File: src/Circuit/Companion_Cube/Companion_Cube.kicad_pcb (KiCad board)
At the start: 2 copper layers, 43.2 x 43.2 mm, 21 parts, among them CON1 AVR-ISP-6, IC1 ATTINY85-S, P1 LED_4, P2 LED_3, P3 LED_2, P4 LED_1, P5 CONN_1, P6 CONN_1, P7 CONN_1, U1 MINI-B_USB

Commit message: Reorganizing
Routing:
- net GND: track 0.00 -> 2.89 mm
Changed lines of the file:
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@@
   (general
     (links 41)
-    (no_connects 1)
+    (no_connects 0)
     (area 175.609956 109.169999 221.3356 152.450001)
     (thickness 1.6)
     (drawings 12)
-    (tracks 76)
+    (tracks 78)
     (zones 0)
     (modules 21)
@@
     (visible_elements 7FFFFFFF)
     (pcbplotparams
-      (layerselection 3178497)
+      (layerselection 284196865)
       (usegerberextensions true)
       (excludeedgelayer true)
@@
       (plotinvisibletext false)
       (padsonsilk false)
-      (subtractmaskfromsilk false)
+      (subtractmaskfromsilk true)
       (outputformat 1)
       (mirror false)
-      (drillshape 1)
+      (drillshape 0)
       (scaleselection 1)
-      (outputdirectory ""))
+      (outputdirectory S:/Users/TyDesktop/Documents/GitHub/3D-LED-Companion-Cube/src/Circuit/Boards/Main/Gerber/))
   )
   (net 0 "")
@@
   (gr_line (start 206.375 139.065) (end 207.645 139.065) (angle 90) (layer Edge.Cuts) (width 0.1))
   (gr_line (start 191.135 139.065) (end 206.375 139.065) (angle 90) (layer Edge.Cuts) (width 0.1))
+  (segment (start 185.05932 132.4102) (end 185.05932 135.16102) (width 0.55) (layer F.Cu) (net 1))
+  (segment (start 185.05932 135.16102) (end 184.96026 135.26008) (width 0.55) (layer F.Cu) (net 1))
   (segment (start 209.55 130.175) (end 209.55 127) (width 0.254) (layer B.Cu) (net 2))
   (segment (start 198.755 120.65) (end 195.58 120.65) (width 0.254) (layer B.Cu) (net 3))

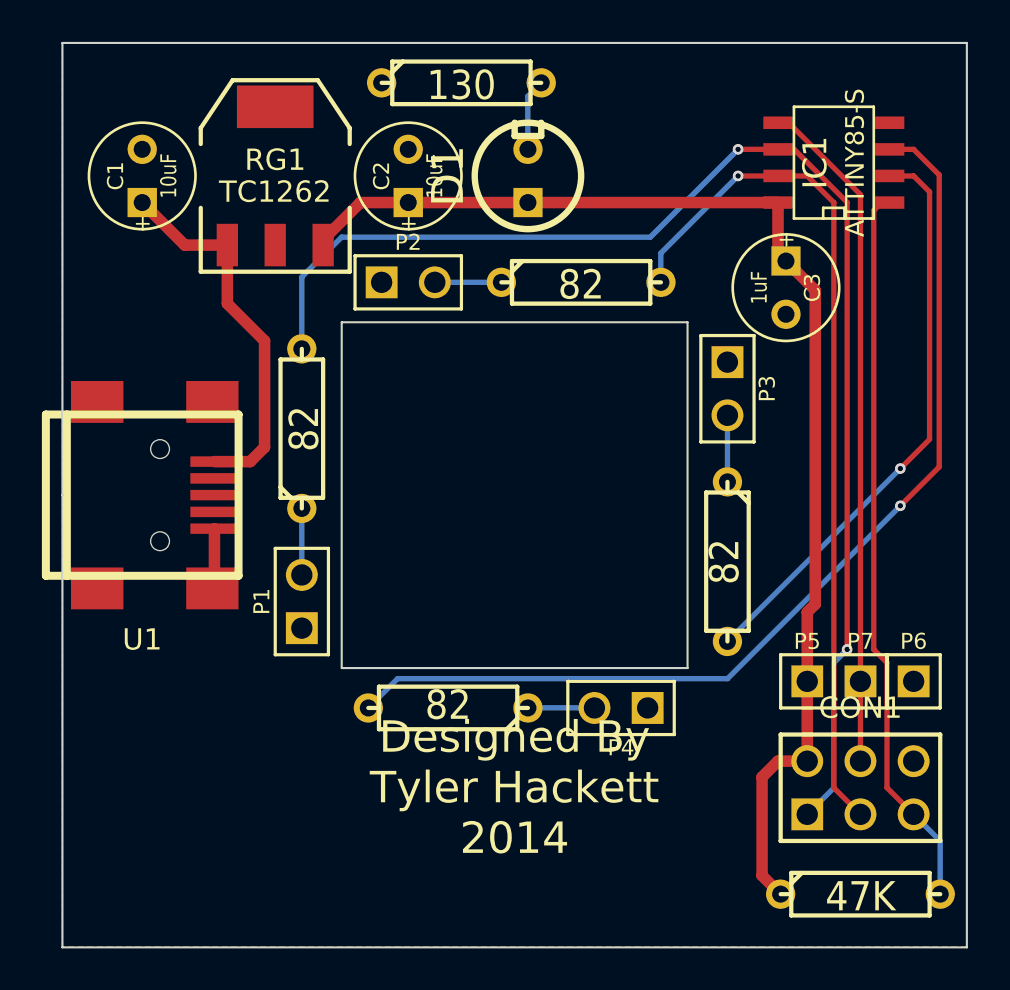
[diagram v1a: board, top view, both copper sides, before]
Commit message: Added attiny85 DIP version
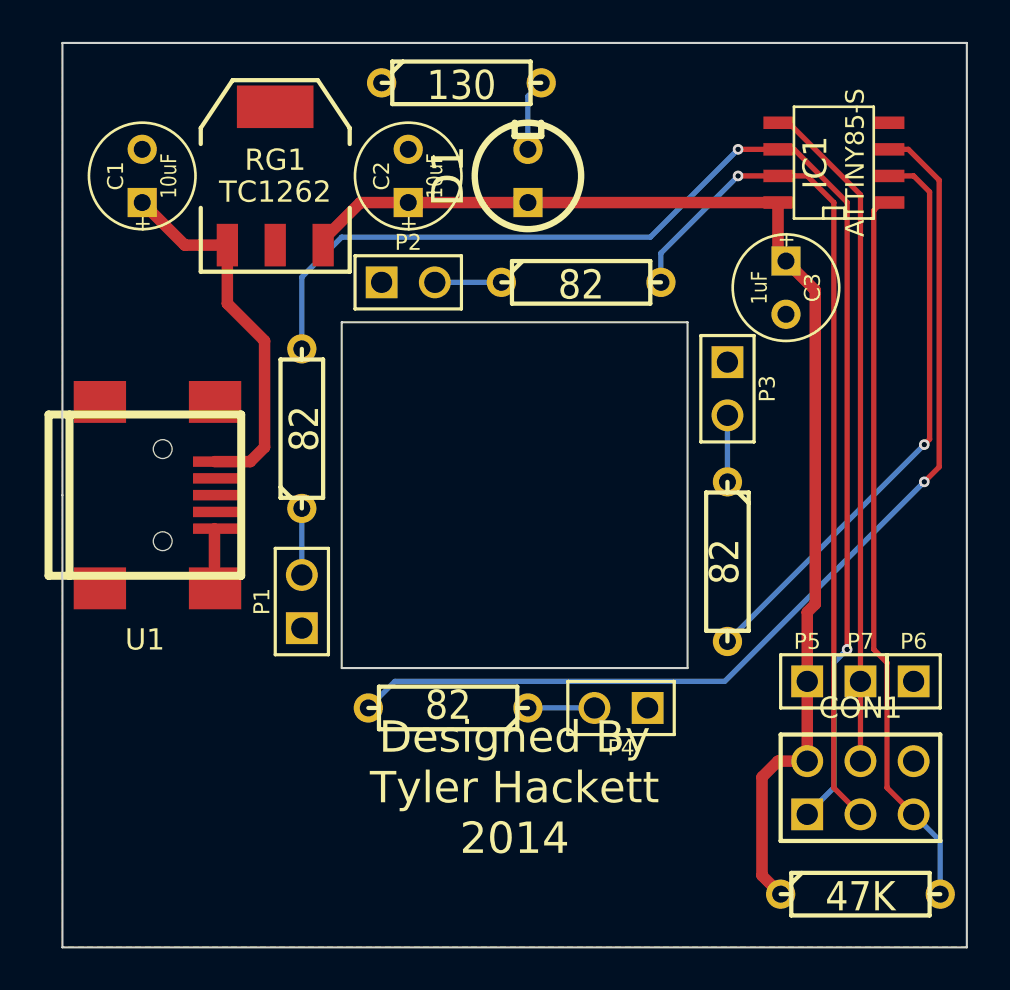
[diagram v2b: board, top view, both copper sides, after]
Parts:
- moved U1 0.13 mm to (181.7, 130.8)
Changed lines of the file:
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@@
     (links 41)
     (no_connects 0)
-    (area 175.609956 109.169999 221.3356 152.450001)
+    (area 175.736956 109.169999 230.603829 152.450001)
     (thickness 1.6)
     (drawings 12)
@@
       (drillshape 0)
       (scaleselection 1)
-      (outputdirectory S:/Users/TyDesktop/Documents/GitHub/3D-LED-Companion-Cube/src/Circuit/Boards/Main/Gerber/))
+      (outputdirectory S:/Users/TyDesktop/Documents/GitHub/3D-LED-Companion-Cube/src/Circuit/Companion_Cube/Gerber/))
   )
   (net 0 "")
@@
   )
   (module USB_MINI_B (layer F.Cu)
-    (at 181.61 130.81)
+    (at 181.737 130.81)
     (descr "USB Mini-B 5-pin SMD connector")
     (tags "USB, Mini-B, connector")
@@
   (segment (start 212.471 113.03) (end 215.9 116.459) (width 0.254) (layer F.Cu) (net 7))
   (segment (start 215.9 143.51) (end 215.9 139.7) (width 0.254) (layer F.Cu) (net 7))
-  (segment (start 192.405 140.97) (end 193.802 139.573) (width 0.254) (layer B.Cu) (net 8))
-  (segment (start 218.44 114.3) (end 217.297 114.3) (width 0.254) (layer F.Cu) (net 8))
-  (segment (start 219.659202 115.519202) (end 218.44 114.3) (width 0.254) (layer F.Cu) (net 8))
-  (segment (start 219.659202 129.463798) (end 219.659202 115.519202) (width 0.254) (layer F.Cu) (net 8))
-  (segment (start 217.805 131.318) (end 219.659202 129.463798) (width 0.254) (layer F.Cu) (net 8))
-  (via (at 217.805 131.318) (size 0.508) (layers F.Cu B.Cu) (net 8))
-  (segment (start 209.55 139.573) (end 217.805 131.318) (width 0.254) (layer B.Cu) (net 8))
-  (segment (start 193.802 139.573) (end 209.55 139.573) (width 0.254) (layer B.Cu) (net 8))
+  (segment (start 217.297 114.3) (end 218.186 114.3) (width 0.254) (layer F.Cu) (net 8))
+  (segment (start 193.675 139.7) (end 192.405 140.97) (width 0.254) (layer B.Cu) (net 8))
+  (segment (start 209.423 139.7) (end 193.675 139.7) (width 0.254) (layer B.Cu) (net 8))
+  (segment (start 218.948 130.175) (end 209.423 139.7) (width 0.254) (layer B.Cu) (net 8))
+  (via (at 218.948 130.175) (size 0.508) (layers F.Cu B.Cu) (net 8))
+  (segment (start 219.659202 129.463798) (end 218.948 130.175) (width 0.254) (layer F.Cu) (net 8))
+  (segment (start 219.659202 115.773202) (end 219.659202 129.463798) (width 0.254) (layer F.Cu) (net 8))
+  (segment (start 218.186 114.3) (end 219.659202 115.773202) (width 0.254) (layer F.Cu) (net 8))
   (segment (start 217.297 115.57) (end 218.44 115.57) (width 0.254) (layer F.Cu) (net 9))
-  (segment (start 217.805 129.54) (end 209.55 137.795) (width 0.254) (layer B.Cu) (net 9))
-  (via (at 217.805 129.54) (size 0.508) (layers F.Cu B.Cu) (net 9))
-  (segment (start 219.202 128.143) (end 217.805 129.54) (width 0.254) (layer F.Cu) (net 9))
+  (segment (start 218.948 128.397) (end 209.55 137.795) (width 0.254) (layer B.Cu) (net 9))
+  (via (at 218.948 128.397) (size 0.508) (layers F.Cu B.Cu) (net 9))
+  (segment (start 219.202 128.143) (end 218.948 128.397) (width 0.254) (layer F.Cu) (net 9))
   (segment (start 219.202 116.332) (end 219.202 128.143) (width 0.254) (layer F.Cu) (net 9))
   (segment (start 218.44 115.57) (end 219.202 116.332) (width 0.254) (layer F.Cu) (net 9))
